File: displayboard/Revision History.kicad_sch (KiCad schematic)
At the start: 0 parts

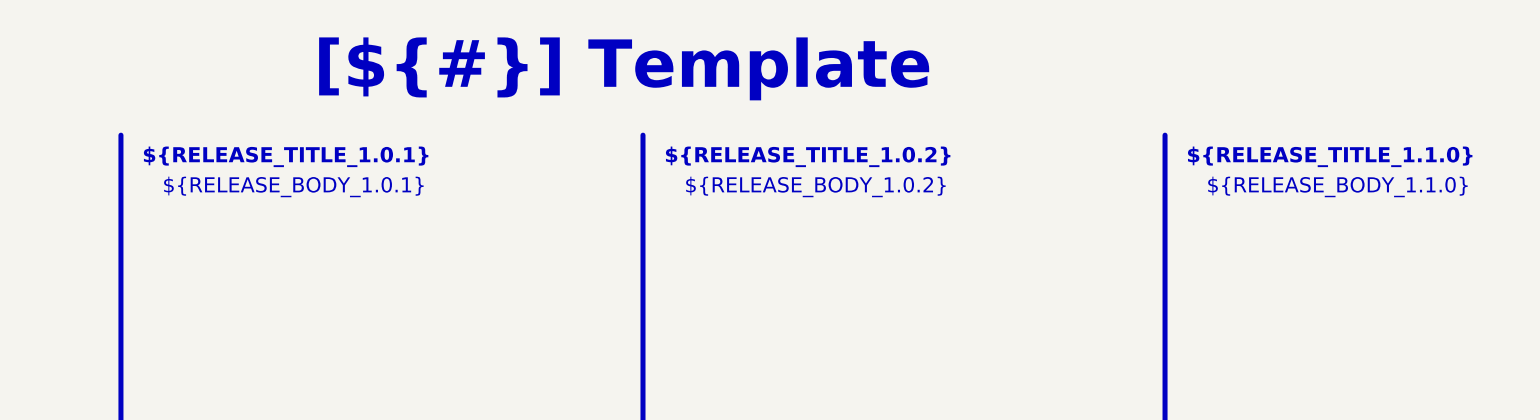
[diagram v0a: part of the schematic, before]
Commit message: Remove old production files, add cutout for the programming cable, add connector for mainboard cable
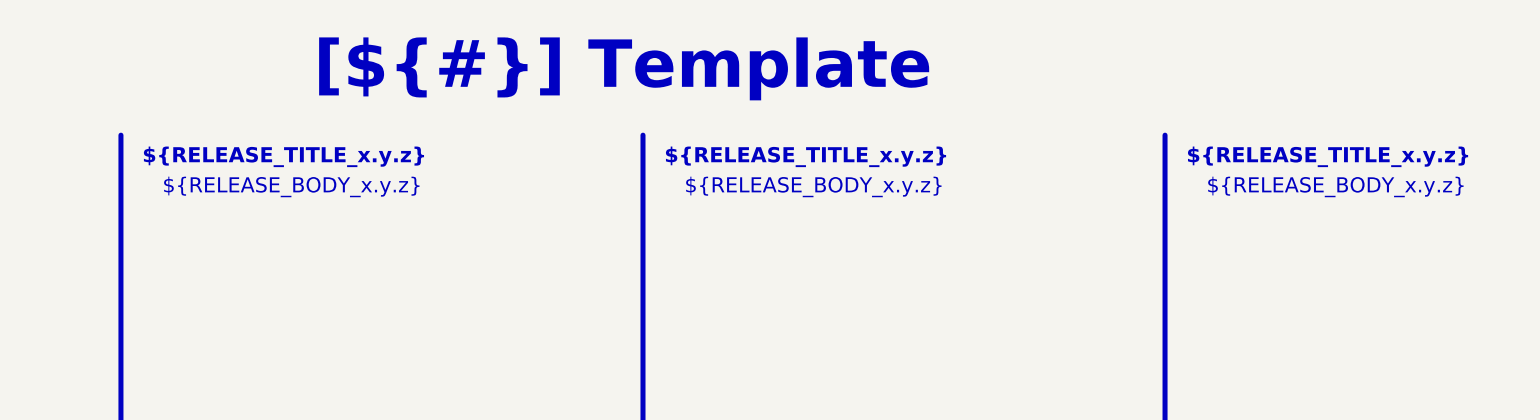
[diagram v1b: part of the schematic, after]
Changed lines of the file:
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@@
 		(company "${COMPANY}")
 	)
-	(text_box "${RELEASE_BODY_1.1.0}"
+	(text_box "${RELEASE_BODY_x.y.z}"
 		(exclude_from_sim no)
 		(at 220.98 35.56 0)
@@
 		(stroke
 			(width -0.0001)
-			(type default)
+			(type solid)
 		)
 		(fill
@@
 		)
 	)
-	(text_box "${RELEASE_TITLE_1.0.2}"
+	(text_box "${RELEASE_TITLE_x.y.z}"
 		(exclude_from_sim no)
 		(at 152.4 31.75 0)
@@
 		(stroke
 			(width -0.0001)
-			(type default)
+			(type solid)
 		)
 		(fill
@@
 		)
 	)
-	(text_box "${RELEASE_BODY_1.0.2}"
+	(text_box "${RELEASE_BODY_x.y.z}"
 		(exclude_from_sim no)
 		(at 154.94 35.56 0)
@@
 		(stroke
 			(width -0.0001)
-			(type default)
+			(type solid)
 		)
 		(fill
@@
 		)
 	)
-	(text_box "${RELEASE_BODY_1.0.1}"
+	(text_box "${RELEASE_BODY_x.y.z}"
 		(exclude_from_sim no)
 		(at 88.9 35.56 0)
@@
 		(stroke
 			(width -0.0001)
-			(type default)
+			(type solid)
 		)
 		(fill
@@
 		)
 	)
-	(text_box "${RELEASE_TITLE_1.0.1}"
+	(text_box "${RELEASE_TITLE_x.y.z}"
 		(exclude_from_sim no)
 		(at 86.36 31.75 0)
@@
 		(stroke
 			(width -0.0001)
-			(type default)
+			(type solid)
 		)
 		(fill
@@
 		)
 	)
-	(text_box "${RELEASE_TITLE_1.1.0}"
+	(text_box "${RELEASE_TITLE_x.y.z}"
 		(exclude_from_sim no)
 		(at 218.44 31.75 0)
@@
 		(stroke
 			(width -0.0001)
-			(type default)
+			(type solid)
 		)
 		(fill
